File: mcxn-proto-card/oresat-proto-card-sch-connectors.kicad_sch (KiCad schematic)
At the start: 13 parts, among them J1 J-SAMTEC-TFM-110-X1-XXX-D-RA, J2 U.FL, J3 U.FL, J4 U.FL, J6 J-SAMTEC-TFM-120-X1-XXX-D-RA

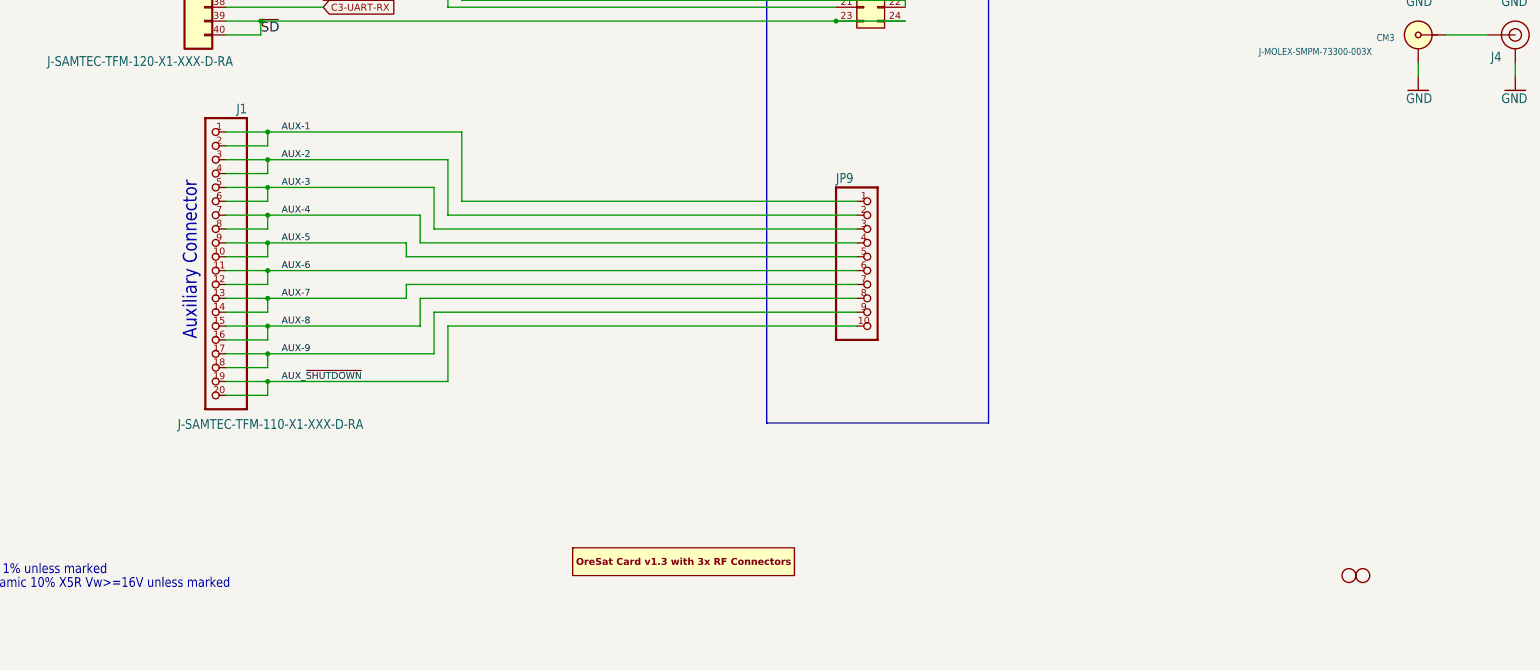
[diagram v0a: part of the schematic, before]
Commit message: Replaced J1 and JP9 w/ OreSat library equivalent
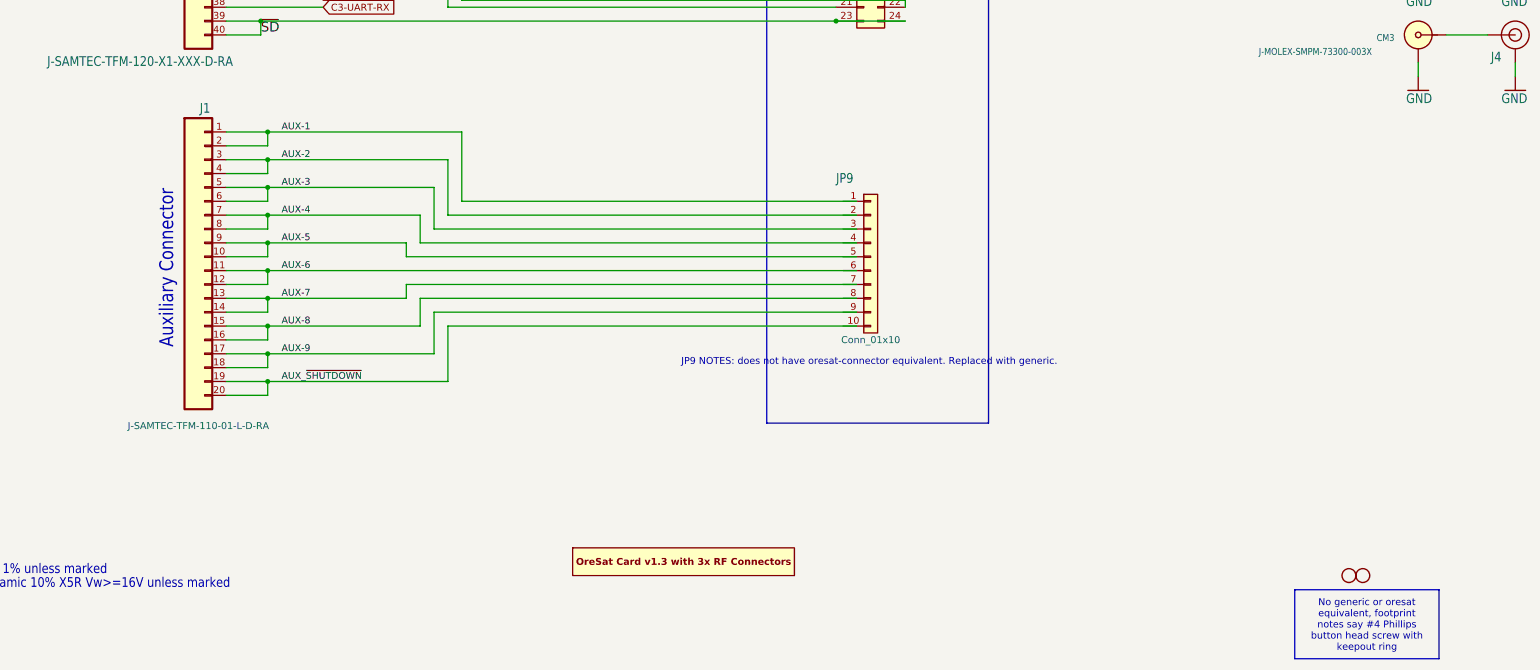
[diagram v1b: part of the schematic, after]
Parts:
- J1: value J-SAMTEC-TFM-110-X1-XXX-D-RA -> J-SAMTEC-TFM-110-01-L-D-RA; footprint oresat-proto-card:J-SAMTEC-TFM-110-X1-XXX-D-RA -> oresat-connectors:J-SAMTEC-TFM-110-X1-XXX-D-RA; symbol oresat-proto-card-eagle-import:J-SAMTEC-TFM-110-X1-XXX-D-RA -> oresat-connectors:J-SAMTEC-TFM-110-01-L-D-RA
- JP9: value PINHD-1X10 -> Conn_01x10; symbol oresat-proto-card-eagle-import:PINHD-1X10 -> Connector_Generic:Conn_01x10
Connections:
- net AUX-1: no longer JP9.1
- net AUX-2: no longer JP9.2
- net AUX-3: no longer JP9.3
- net AUX-4: no longer JP9.4
- net AUX-5: no longer JP9.5
- net AUX-6: no longer JP9.6
- net AUX-7: no longer JP9.7
- net AUX-8: no longer JP9.8
- net AUX-9: no longer JP9.9
- net AUX_~{SHUTDOWN}: no longer JP9.10
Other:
- note added: "JP9 NOTES: does not have oresat-connector equivalent. Replaced with generic."
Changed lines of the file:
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@@
 	(title_block
 		(title "OreSat M0 Proto Card: Connectors")
-		(date "2024-03-21")
+		(date "2025-06-29")
 		(rev "5.0")
 	)
 	(text "Auxiliary Connector"
 		(exclude_from_sim no)
-		(at 73.66 203.2 90)
+		(at 69.342 204.724 90)
 		(effects
 			(font
@@
 		)
 	)
+	(text "JP9 NOTES: does not have oresat-connector equivalent. Replaced with generic."
+		(exclude_from_sim no)
+		(at 196.596 207.264 0)
+		(effects
+			(font
+				(size 1.27 1.27)
+			)
+		)
+	)
 	(text "RF connections and test points"
 		(exclude_from_sim no)
@@
 		)
 	)
+	(text_box "No generic or oresat equivalent, footprint notes say #4 Phillips button head screw with keepout ring"
+		(exclude_from_sim no)
+		(at 274.5573 248.978 0)
+		(size 26.4327 12.642)
+		(margins 0.9525 0.9525 0.9525 0.9525)
+		(stroke
+			(width 0)
+			(type default)
+		)
+		(fill
+			(type none)
+		)
+		(effects
+			(font
+				(size 1.27 1.27)
+			)
+		)
+	)
 	(junction
 		(at 190.5 137.16)
@@
 	)
 	(symbol
-		(lib_id "oresat-proto-card-eagle-import:PINHD-1X10")
+		(lib_id "Connector_Generic:Conn_01x10")
 		(at 196.85 187.96 0)
 		(unit 1)
@@
 			)
 		)
-		(property "Value" "PINHD-1X10"
-			(at 190.5 205.74 0)
+		(property "Value" "Conn_01x10"
+			(at 196.85 203.2 0)
 			(effects
 				(font
-					(size 1.778 1.5113)
+					(size 1.27 1.27)
 				)
-				(justify left bottom)
-				(hide yes)
 			)
 		)
@@
 			)
 		)
-		(property "Datasheet" ""
+		(property "Datasheet" "~"
 			(at 196.85 187.96 0)
 			(effects
@@
 			)
 		)
-		(property "Description" ""
+		(property "Description" "Generic connector, single row, 01x10, script generated (kicad-library-utils/schlib/autogen/connector/)"
 			(at 196.85 187.96 0)
 			(effects
@@
 					(size 1.27 1.27)
 				)
+				(hide yes)
 			)
 		)
@@
 	)
 	(symbol
-		(lib_id "oresat-proto-card-eagle-import:J-SAMTEC-TFM-110-X1-XXX-D-RA")
-		(at 76.2 187.96 0)
-		(mirror y)
+		(lib_id "oresat-connectors:J-SAMTEC-TFM-110-01-L-D-RA")
+		(at 73.66 190.5 0)
 		(unit 1)
 		(exclude_from_sim no)
@@
 		(dnp no)
 		(property "Reference" "J1"
-			(at 82.55 161.925 0)
+			(at 73.914 161.798 0)
 			(effects
 				(font
@@
 			)
 		)
-		(property "Value" "J-SAMTEC-TFM-110-X1-XXX-D-RA"
-			(at 69.85 219.71 0)
+		(property "Value" "J-SAMTEC-TFM-110-01-L-D-RA"
+			(at 73.66 218.948 0)
 			(effects
 				(font
-					(size 1.778 1.5113)
+					(size 1.27 1.27)
 				)
-				(justify right bottom)
 			)
 		)
-		(property "Footprint" "oresat-proto-card:J-SAMTEC-TFM-110-X1-XXX-D-RA"
-			(at 76.2 187.96 0)
+		(property "Footprint" "oresat-connectors:J-SAMTEC-TFM-110-X1-XXX-D-RA"
+			(at 78.74 250.19 0)
 			(effects
 				(font
@@
 			)
 		)
-		(property "Datasheet" ""
-			(at 76.2 187.96 0)
+		(property "Datasheet" "https://suddendocs.samtec.com/catalog_english/tfm.pdf"
+			(at 76.2 254 0)
 			(effects
 				(font
@@
 			)
 		)
-		(property "Description" ""
-			(at 76.2 187.96 0)
+		(property "Description" "OreSat backplane connector, 2x20 RA"
+			(at 73.66 190.5 0)
 			(effects
 				(font
 					(size 1.27 1.27)
 				)
+				(hide yes)
 			)
 		)
 		(property "DIS" "Digikey"
-			(at 76.2 187.96 0)
+			(at 73.66 190.5 0)
 			(effects
 				(font
@@
 		)
 		(property "DPN" "SAM10113-ND"
-			(at 76.2 187.96 0)
+			(at 73.66 190.5 0)
 			(effects
 				(font
@@
 		)
 		(property "MFR" "Samtec"
-			(at 76.2 187.96 0)
+			(at 73.66 190.5 0)
 			(effects
 				(font
@@
 		)
 		(property "MPN" "TFM-110-01-L-D-RA "
-			(at 76.2 187.96 0)
+			(at 73.66 190.5 0)
 			(effects
 				(font

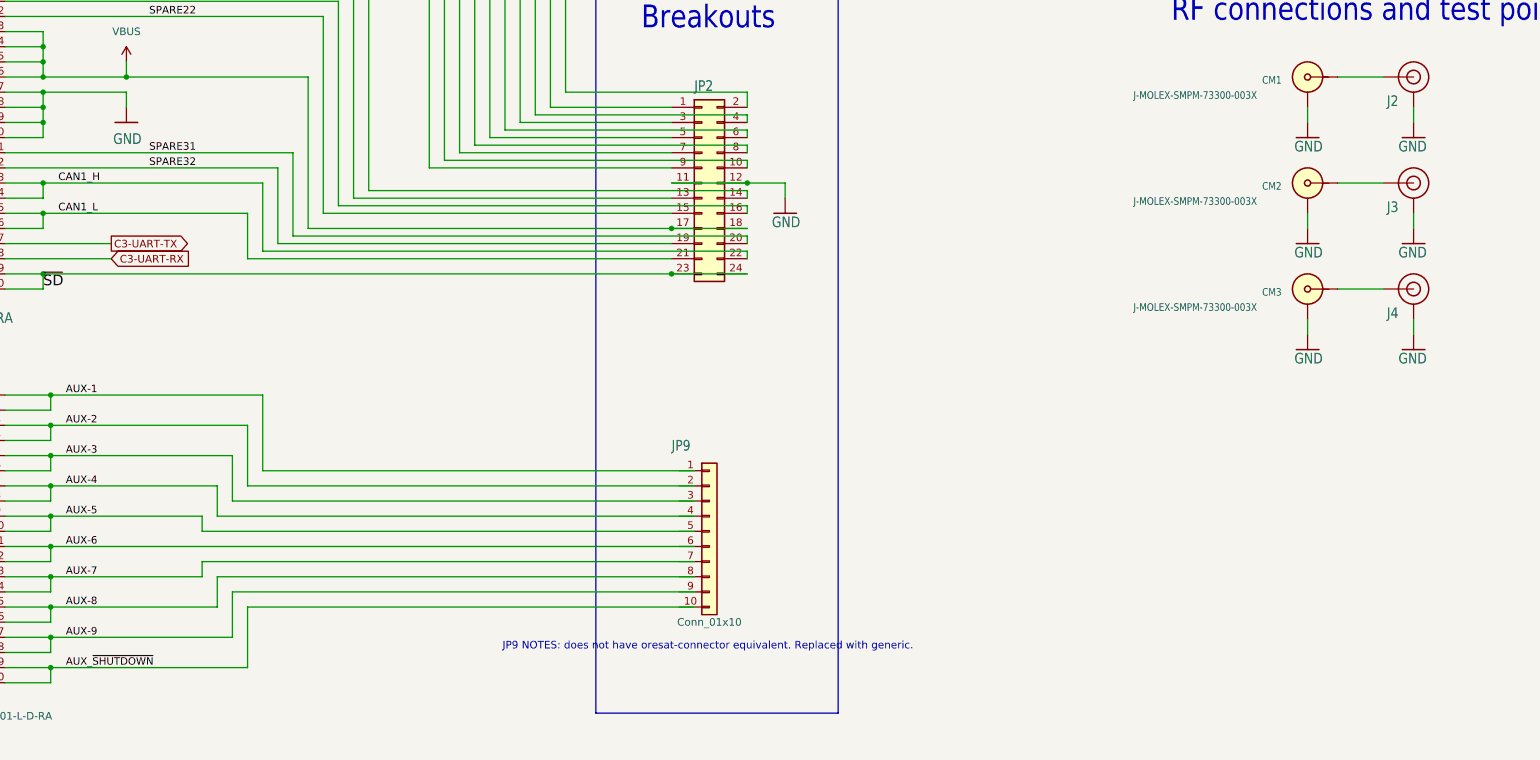
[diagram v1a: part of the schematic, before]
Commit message: Removed and replaced eagle libraries for C, R, and Power symbols
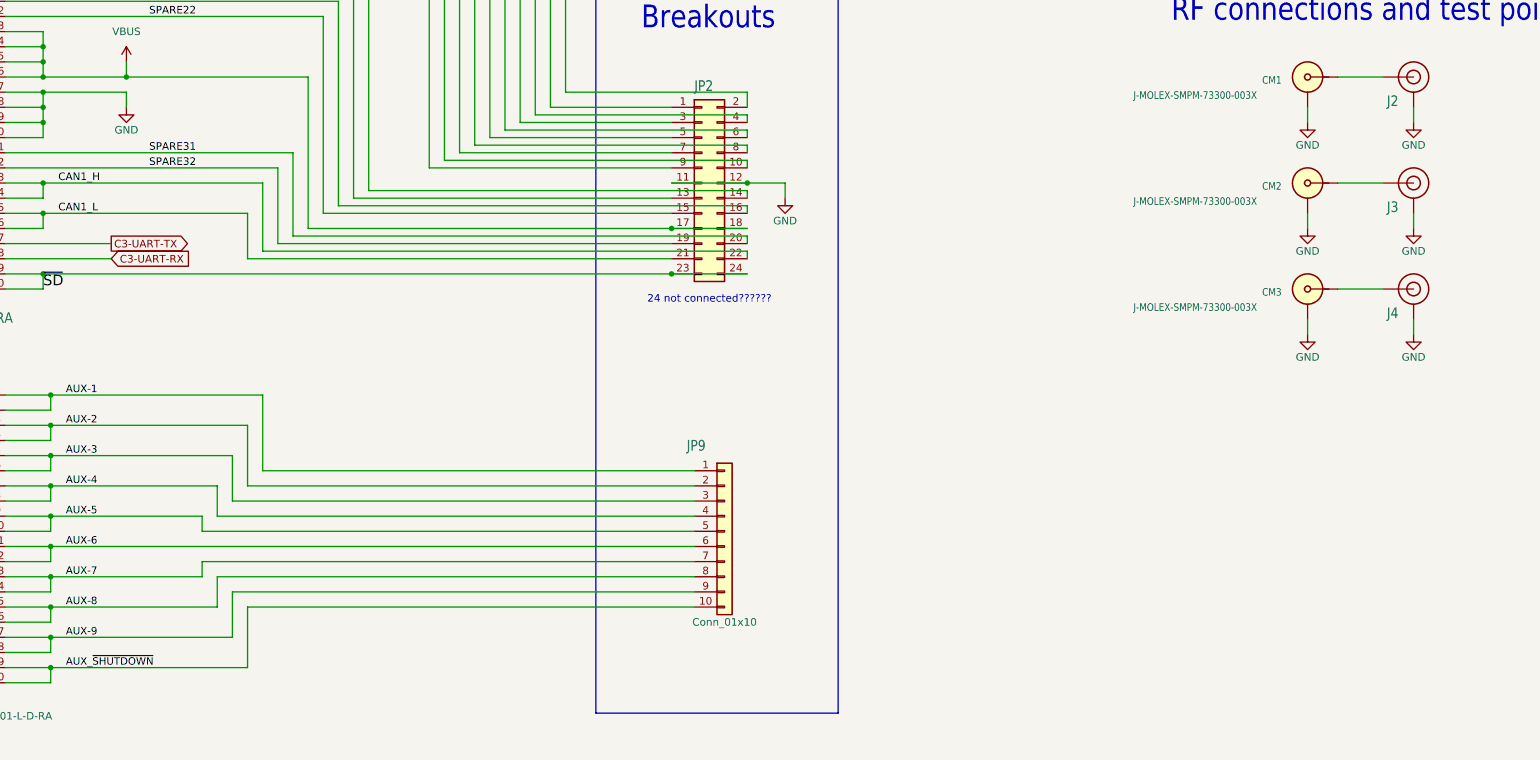
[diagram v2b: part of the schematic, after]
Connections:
- net AUX-1: now also JP9.1 (Pin_1)
- net AUX-2: now also JP9.2 (Pin_2)
- net AUX-3: now also JP9.3 (Pin_3)
- net AUX-4: now also JP9.4 (Pin_4)
- net AUX-5: now also JP9.5 (Pin_5)
- net AUX-6: now also JP9.6 (Pin_6)
- net AUX-7: now also JP9.7 (Pin_7)
- net AUX-8: now also JP9.8 (Pin_8)
- net AUX-9: now also JP9.9 (Pin_9)
- net AUX_~{SHUTDOWN}: now also JP9.10 (Pin_10)
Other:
- note added: "24 not connected??????"
- note removed: "JP9 NOTES: does not have oresat-connector equivalent. Replaced with generic."
- moved on the sheet: JP9

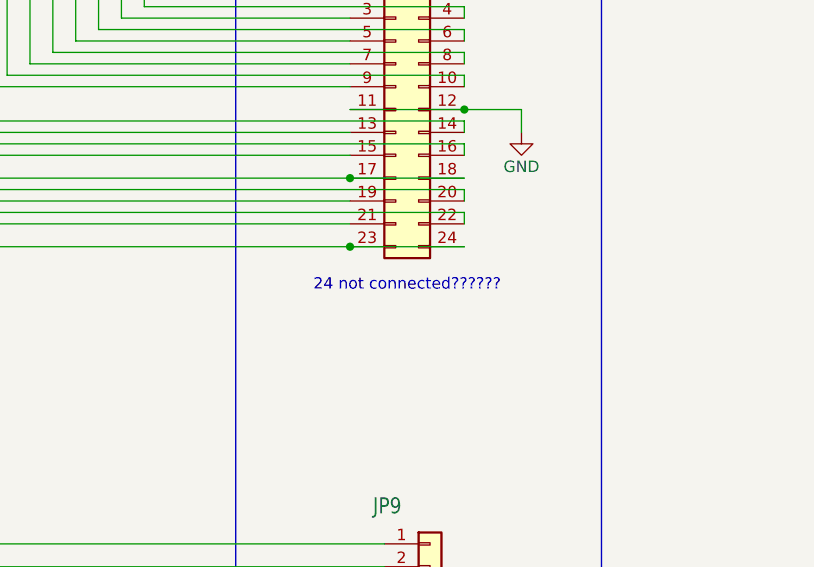
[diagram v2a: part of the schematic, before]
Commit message: Removed and replaced Eagle libraries for MOSFET
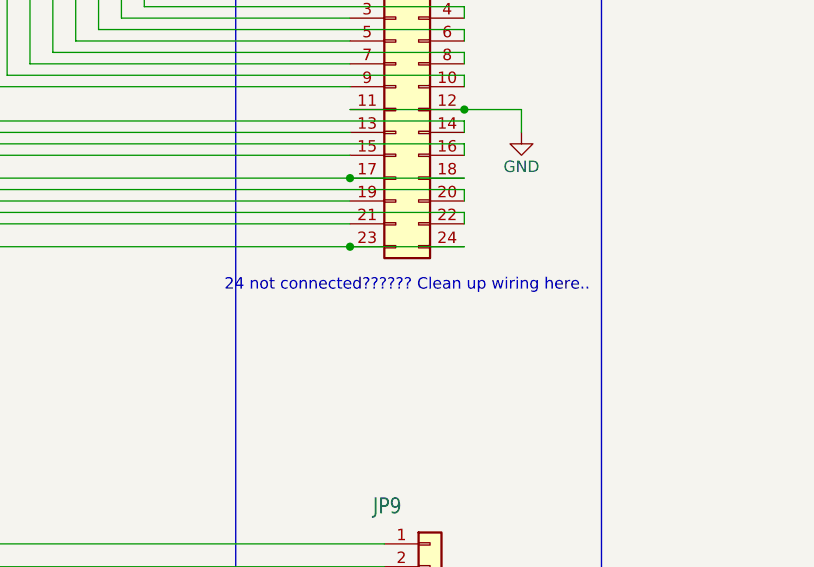
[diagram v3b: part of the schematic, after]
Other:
- note added: "24 not connected?????? Clean up wiring here.."
- note removed: "24 not connected??????"
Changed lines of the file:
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@@
 		)
 	)
-	(text "24 not connected??????"
+	(text "24 not connected?????? Clean up wiring here.."
 		(exclude_from_sim no)
 		(at 196.85 149.098 0)
